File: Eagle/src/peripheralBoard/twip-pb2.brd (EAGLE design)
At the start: 94.9 x 72.4 mm, 31 parts, among them J1 UJ2-BH-1-TH, Q2 IRFD9120

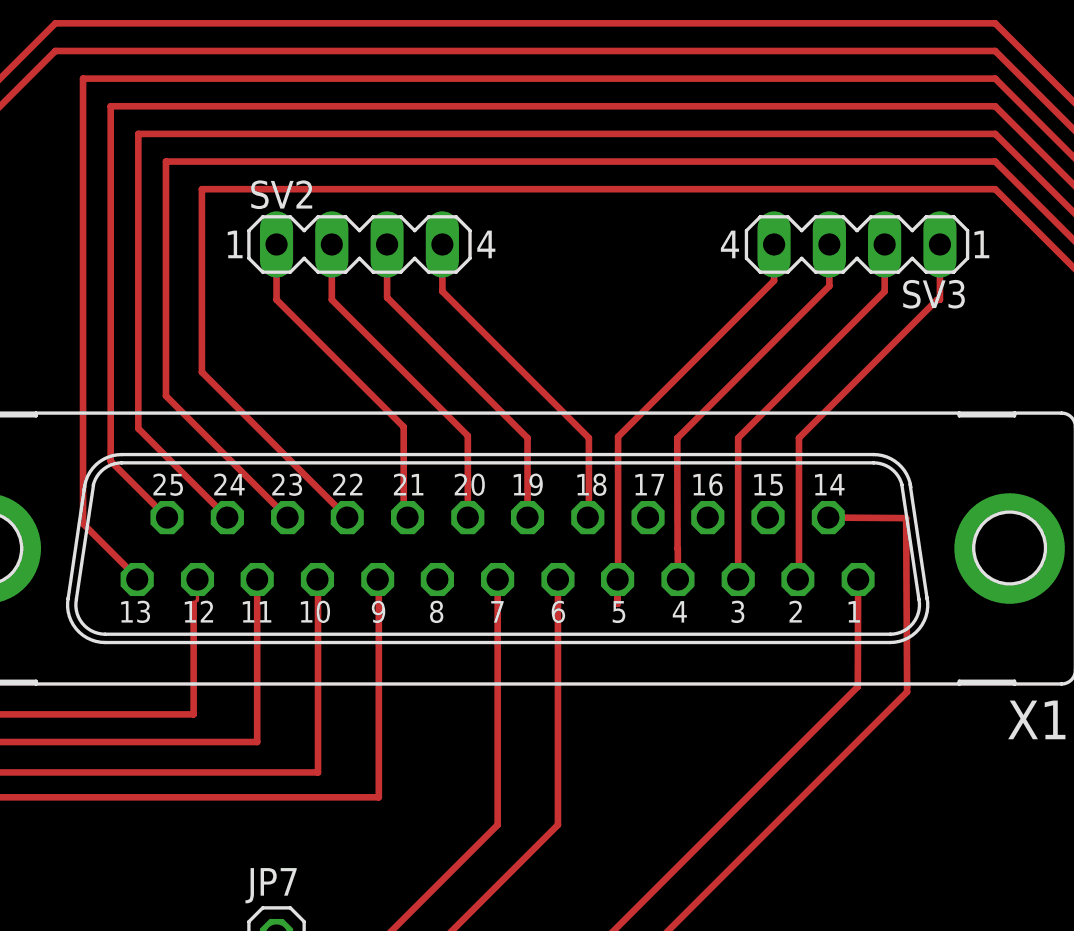
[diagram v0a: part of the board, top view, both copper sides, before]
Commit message: Update twip-pb2.brd
fix USB data connections
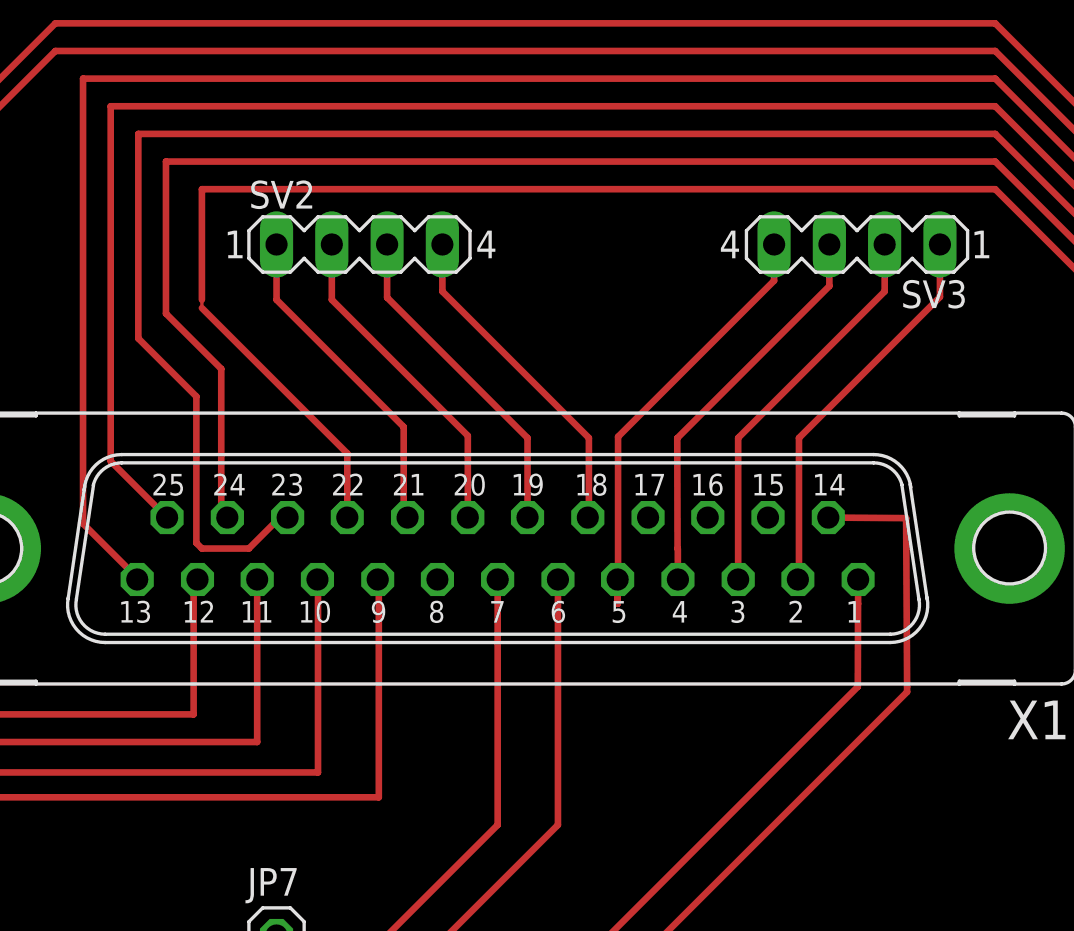
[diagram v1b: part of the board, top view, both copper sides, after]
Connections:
- net N$22: now also X1.23; no longer X1.24
- net N$23: now also X1.24; no longer X1.23
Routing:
- net N$22: track 145.0 -> 150.5 mm
- net N$23: track 144.7 -> 143.5 mm
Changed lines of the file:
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@@
 <contactref element="X1" pad="1"/>
 <wire x1="50.8" y1="22.86" x2="27.94" y2="22.86" width="0.3048" layer="1"/>
-<wire x1="72.4408" y1="45.5676" x2="72.4266" y2="40.63989375" width="0.3048" layer="1"/>
+<wire x1="72.437578125" y1="44.4498625" x2="72.4266" y2="40.63989375" width="0.3048" layer="1"/>
 <wire x1="58.6486" y1="34.29" x2="51.0286" y2="26.67" width="0.3048" layer="1"/>
 <wire x1="51.0286" y1="26.67" x2="50.8" y2="26.67" width="0.3048" layer="1"/>
@@
 <wire x1="72.4266" y1="40.63989375" x2="54.64670625" y2="22.86" width="0.3048" layer="1"/>
 <wire x1="54.64670625" y1="22.86" x2="50.8" y2="22.86" width="0.3048" layer="1"/>
+<wire x1="72.4408" y1="45.5676" x2="72.4408" y2="44.453084375" width="0.3048" layer="1"/>
+<wire x1="72.4408" y1="44.453084375" x2="72.437578125" y2="44.4498625" width="0.1524" layer="1"/>
 </signal>
 <signal name="N$21">
@@
 <contactref element="X1" pad="11"/>
 <wire x1="78.74" y1="71.12" x2="35.56" y2="71.12" width="0.3048" layer="1"/>
-<wire x1="44.831" y1="45.5676" x2="44.831" y2="38.1" width="0.3048" layer="1"/>
+<wire x1="44.831" y1="44.45" x2="44.831" y2="38.1" width="0.3048" layer="1"/>
 <wire x1="44.831" y1="38.1" x2="26.67" y2="38.1" width="0.3048" layer="1"/>
 <wire x1="26.67" y1="62.23" x2="26.67" y2="38.1" width="0.3048" layer="1"/>
 <wire x1="35.56" y1="71.12" x2="26.67" y2="62.23" width="0.3048" layer="1"/>
+<wire x1="44.831" y1="45.5676" x2="44.831" y2="44.45" width="0.3048" layer="1"/>
 </signal>
 <signal name="N$28">
@@
 <contactref element="X1" pad="13"/>
 <wire x1="36.83" y1="68.58" x2="78.74" y2="68.58" width="0.3048" layer="1"/>
-<wire x1="39.3192" y1="45.5676" x2="39.1668" y2="45.72" width="0.3048" layer="1"/>
 <wire x1="39.3192" y1="45.5676" x2="39.3192" y2="45.6438" width="0.3048" layer="1"/>
 <wire x1="39.3192" y1="45.6438" x2="36.83" y2="48.133" width="0.3048" layer="1"/>
@@
 <contactref element="X1" pad="12"/>
 <wire x1="78.74" y1="69.85" x2="35.56" y2="69.85" width="0.3048" layer="1"/>
-<wire x1="41.91" y1="44.45" x2="41.91" y2="39.37" width="0.3048" layer="1"/>
 <wire x1="41.91" y1="39.37" x2="27.94" y2="39.37" width="0.3048" layer="1"/>
 <wire x1="27.94" y1="62.23" x2="27.94" y2="39.37" width="0.3048" layer="1"/>
 <wire x1="35.56" y1="69.85" x2="27.94" y2="62.23" width="0.3048" layer="1"/>
-<wire x1="42.0878" y1="45.5676" x2="42.0878" y2="44.6278" width="0.1524" layer="1"/>
-<wire x1="42.0878" y1="44.6278" x2="41.91" y2="44.45" width="0.1524" layer="1"/>
+<wire x1="42.0878" y1="45.5676" x2="41.91" y2="45.3898" width="0.3048" layer="1"/>
+<wire x1="41.91" y1="45.3898" x2="41.91" y2="39.37" width="0.3048" layer="1"/>
 </signal>
 <signal name="N$6">
@@
 <wire x1="39.37" y1="66.04" x2="78.74" y2="66.04" width="0.3048" layer="1"/>
 <wire x1="75.946" y1="17.78" x2="69.596" y2="11.43" width="0.3048" layer="1"/>
-<contactref element="X1" pad="24"/>
-<wire x1="43.4594" y1="48.4124" x2="39.37" y2="52.5018" width="0.3048" layer="1"/>
-<wire x1="39.37" y1="52.5018" x2="39.37" y2="66.04" width="0.3048" layer="1"/>
+<contactref element="X1" pad="23"/>
+<wire x1="39.37" y1="56.642" x2="39.37" y2="66.04" width="0.3048" layer="1"/>
+<wire x1="46.228" y1="48.4124" x2="45.8724" y2="48.4124" width="0.3048" layer="1"/>
+<wire x1="45.8724" y1="48.4124" x2="44.45" y2="46.99" width="0.3048" layer="1"/>
+<wire x1="44.45" y1="46.99" x2="42.291" y2="46.99" width="0.3048" layer="1"/>
+<wire x1="42.037" y1="47.244" x2="42.037" y2="53.975" width="0.3048" layer="1"/>
+<wire x1="42.037" y1="53.975" x2="39.37" y2="56.642" width="0.3048" layer="1"/>
+<wire x1="42.291" y1="46.99" x2="42.037" y2="47.244" width="0.3048" layer="1"/>
 </signal>
 <signal name="N$23">
@@
 <wire x1="40.64" y1="64.77" x2="78.74" y2="64.77" width="0.3048" layer="1"/>
 <wire x1="68.58" y1="12.7" x2="74.93" y2="19.05" width="0.3048" layer="1"/>
-<contactref element="X1" pad="23"/>
-<wire x1="46.228" y1="48.4124" x2="40.64" y2="54.0004" width="0.3048" layer="1"/>
-<wire x1="40.64" y1="54.0004" x2="40.64" y2="64.77" width="0.3048" layer="1"/>
+<contactref element="X1" pad="24"/>
+<wire x1="40.64" y1="57.785" x2="40.64" y2="64.77" width="0.3048" layer="1"/>
+<wire x1="40.64" y1="57.785" x2="43.18" y2="55.245" width="0.3048" layer="1"/>
+<wire x1="43.18" y1="55.245" x2="43.18" y2="48.6918" width="0.3048" layer="1"/>
+<wire x1="43.18" y1="48.6918" x2="43.4594" y2="48.4124" width="0.3048" layer="1"/>
 </signal>
 <signal name="N$24">
@@
 <wire x1="46.99" y1="13.97" x2="53.34" y2="20.32" width="0.3048" layer="1"/>
 <contactref element="X1" pad="22"/>
-<wire x1="48.9712" y1="48.4124" x2="42.291" y2="55.0926" width="0.3048" layer="1"/>
-<wire x1="42.291" y1="55.0926" x2="42.291" y2="63.5" width="0.3048" layer="1"/>
+<wire x1="42.291" y1="58.42" x2="42.291" y2="63.5" width="0.3048" layer="1"/>
+<wire x1="48.9712" y1="48.4124" x2="48.9712" y2="51.3588" width="0.3048" layer="1"/>
+<wire x1="42.291" y1="58.039" x2="42.291" y2="58.42" width="0.1524" layer="1"/>
+<wire x1="48.9712" y1="51.3588" x2="42.291" y2="58.039" width="0.3048" layer="1"/>
 </signal>
 <signal name="N$4">
@@
 <contactref element="R1" pad="2"/>
 <contactref element="X1" pad="10"/>
-<wire x1="47.625" y1="36.703" x2="47.625" y2="45.5422" width="0.3048" layer="1"/>
-<wire x1="47.625" y1="45.5422" x2="47.5996" y2="45.5676" width="0.3048" layer="1"/>
+<wire x1="47.625" y1="45.5422" x2="47.625" y2="36.703" width="0.3048" layer="1"/>
 <wire x1="20.32" y1="44.45" x2="21.59" y2="44.45" width="0.3048" layer="1"/>
 <wire x1="21.59" y1="44.45" x2="25.4" y2="40.64" width="0.3048" layer="1"/>
@@
 <wire x1="16.51" y1="52.07" x2="16.51" y2="44.45" width="0.3048" layer="1"/>
 <wire x1="16.51" y1="44.45" x2="20.32" y2="44.45" width="0.3048" layer="1"/>
+<wire x1="47.5996" y1="45.5676" x2="47.625" y2="45.5422" width="0.1524" layer="1"/>
 </signal>
 <signal name="N$25">
@@
 <contactref element="SV3" pad="1"/>
 <wire x1="69.6722" y1="45.5676" x2="69.723" y2="45.6184" width="0.3048" layer="1"/>
-<wire x1="76.2" y1="58.42" x2="76.2" y2="60.96" width="0.3048" layer="1"/>
 <wire x1="69.723" y1="45.6184" x2="69.723" y2="52.07" width="0.3048" layer="1"/>
-<wire x1="69.723" y1="52.07" x2="76.073" y2="58.42" width="0.3048" layer="1"/>
-<wire x1="76.073" y1="58.42" x2="76.2" y2="58.42" width="0.3048" layer="1"/>
+<wire x1="76.2" y1="58.547" x2="76.2" y2="60.96" width="0.3048" layer="1"/>
+<wire x1="69.723" y1="52.07" x2="76.2" y2="58.547" width="0.3048" layer="1"/>
 </signal>
 <signal name="N$15">
@@
 <wire x1="22.86" y1="40.64" x2="22.86" y2="36.83" width="0.3048" layer="1"/>
 <contactref element="X1" pad="9"/>
-<wire x1="50.419" y1="35.56" x2="50.419" y2="45.5168" width="0.3048" layer="1"/>
-<wire x1="50.419" y1="45.5168" x2="50.3682" y2="45.5676" width="0.3048" layer="1"/>
+<wire x1="50.419" y1="45.5168" x2="50.419" y2="35.56" width="0.3048" layer="1"/>
 <wire x1="50.419" y1="35.56" x2="24.13" y2="35.56" width="0.3048" layer="1"/>
 <wire x1="22.86" y1="36.83" x2="24.13" y2="35.56" width="0.3048" layer="1"/>
+<wire x1="50.3682" y1="45.5676" x2="50.419" y2="45.5168" width="0.1524" layer="1"/>
 </signal>
 <signal name="N$11">
